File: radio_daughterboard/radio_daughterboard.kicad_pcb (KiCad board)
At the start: 4 copper layers, 120 x 40.5 mm, 126 parts, among them J1 DF40C 60-pin radio daughterbo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, J240 2m/VHF internal/PCB antenna f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, J241 2m/VHF rear external SMA/u.FL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, J250 70cm/UHF internal/PCB antenna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, J251 70cm/UHF rear external SMA/u.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, J42 GNSS passive antenna U.FL, J70 DRA818V 2m FM module, J71 DRA818U 70cm FM module, Q330 2N7002KT1G VHF PTT/suspend fa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, Q331 2N7002KT1G UHF PTT/suspend fa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, Q332 BSS84LT1G codec-loss force-mu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, U1 AP2112K-3.3 600mA daughterboa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, U240 PE42820B-X 2m/VHF 43dBm-CW RF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, U241 SN74LVC1G373DCKR VHF transmit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, U242 SN74LVC3G34DCUR VHF fail-safe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, U243 SN74LVC1T45 VHF TXD 4V-to-3V3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, U250 PE42820B-X 70cm/UHF 43dBm-CW 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, U251 SN74LVC1G373DCKR UHF transmit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, U252 SN74LVC3G34DCUR UHF fail-safe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, U253 SN74LVC1T45 UHF TXD 4V-to-3V3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, U260 SN74LVC2G04DCKR PTT request i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, U261 SN74LVC2G32DCUR dual-radio PT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, U330 PCM2902CDBR USB audio codec, U40 MAX-M10S GNSS, U41 SN74LVC3G34 GNSS input isolat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, U70 TPS54302 RADIO_DB_5V -> RADIO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, Y330 ABM8G-106-12.000MHZ-T 12MHz 1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

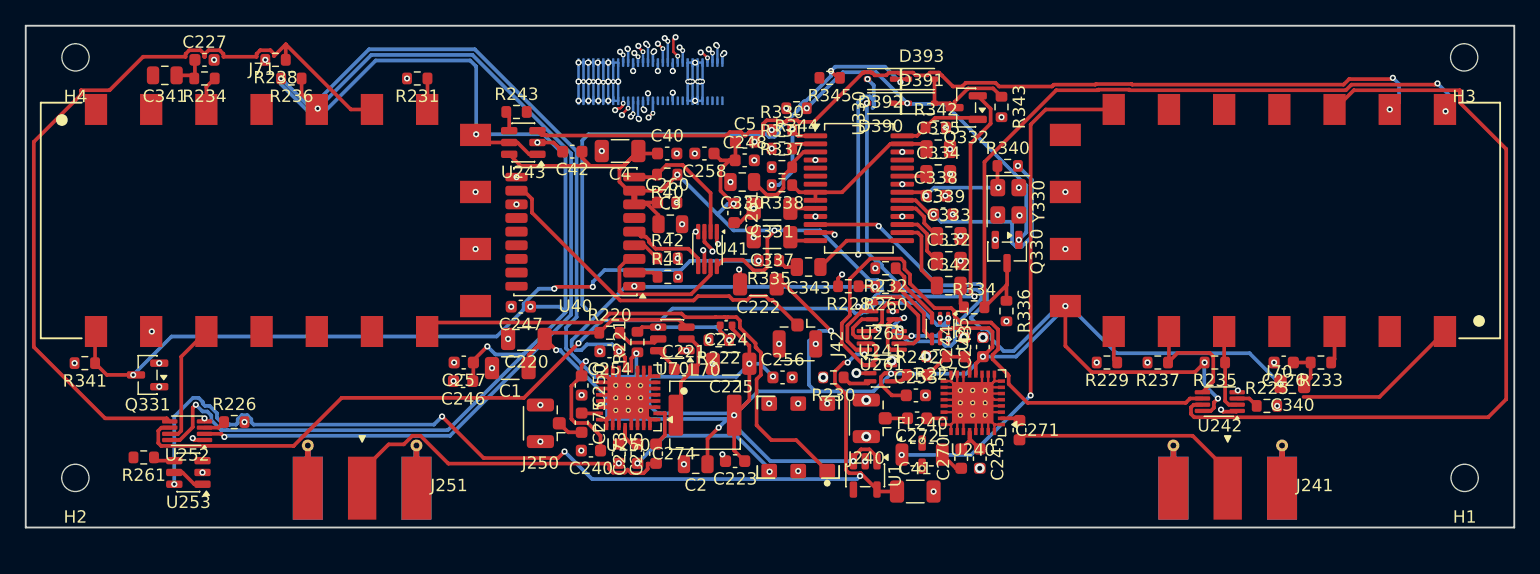
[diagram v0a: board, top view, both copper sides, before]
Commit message: Fix 3D model paths and update PCB format to KiCad 10.0
- Update 3D model paths in radio and keyboard daughterboards to use KIPRJMOD
- Replace Cherry MX ULP STEP model with corrected version
- Add Hirose DF40C and ublox MAX-7Q 3D STEP models
- Fix 3D model offset scripts for mezzanine connector stack
- Auto-format integer-to-float notation from KiCad 10.0 save
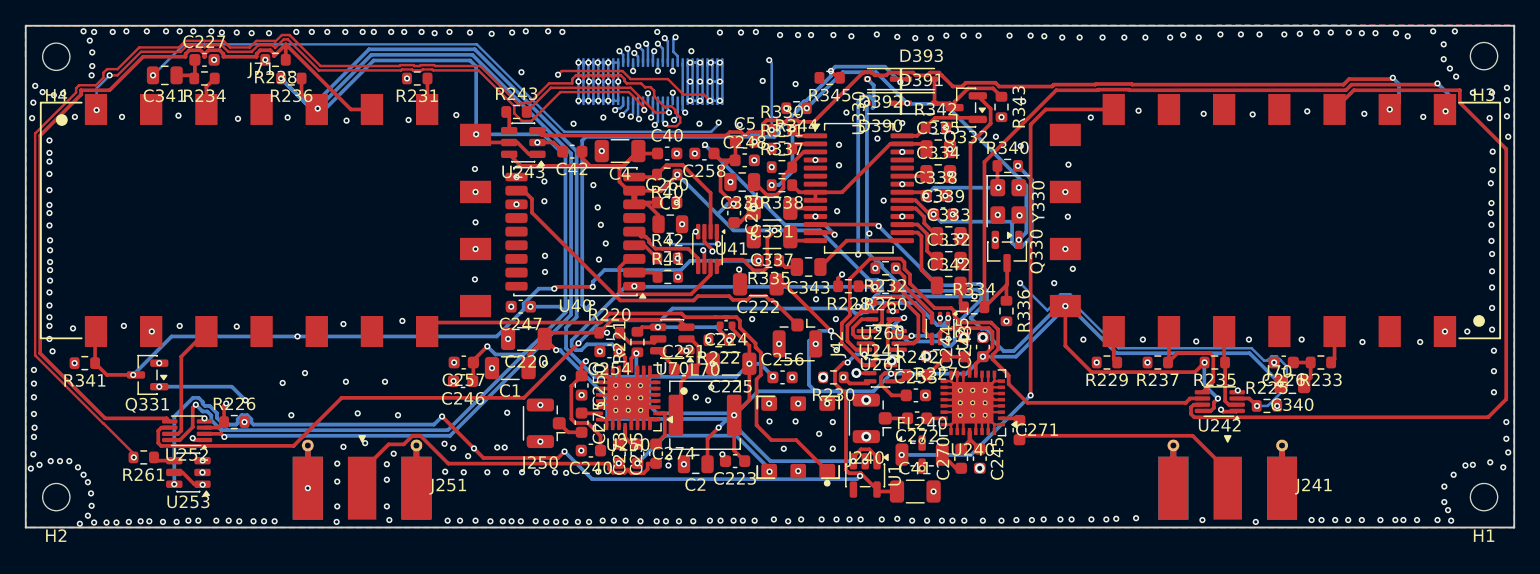
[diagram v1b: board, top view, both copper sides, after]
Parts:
- moved H1 2.20 mm to (207.7, 122.6)
- moved H2 2.18 mm to (92.6, 122.6)
- moved H3 1.60 mm to (207.7, 87.0)
- moved H4 1.55 mm to (92.6, 87.1)
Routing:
- net /RADIO_VHF_UART_TX: track 3.47 -> 102.2 mm
- net /RADIO_UHF_UART_RX: track 0.00 -> 95.8 mm, vias 0 -> 2
- net /RADIO_VHF_PD_N: track 3.32 -> 72.6 mm, vias 1 -> 3
- net /RADIO_VHF_SQL: track 15.1 -> 80.8 mm, vias 1 -> 2
- net /USB Radio Audio/CODEC_LINEIN_R: track 1.62 -> 67.3 mm, vias 1 -> 4
- net /RADIO_UHF_UART_TX: track 2.70 -> 65.4 mm
- net /RADIO_UHF_PD_N: track 3.34 -> 63.8 mm, vias 1 -> 2
- net /RADIO_VHF_RF_SEL_3V3: track 3.38 -> 61.6 mm, vias 1 -> 2
- net /RADIO_UHF_SQL: track 0.86 -> 53.9 mm, vias 1 -> 3
- net /RADIO_DB_5V: track 57.2 -> 105.0 mm, vias 7 -> 11
- net /USB Radio Audio/UHF_MUTE_GATE: track 45.5 -> 84.7 mm, vias 3 -> 5
- net /RADIO_UHF_RF_SEL_3V3: track 6.78 -> 35.2 mm, vias 1 -> 2
- net /GNSS_UART_TX: track 2.18 -> 29.7 mm, vias 2 -> 3
- net /RADIO_VHF_PTT_N: track 39.1 -> 66.4 mm, vias 2 -> 4
- net /GNSS_PPS: track 0.97 -> 24.6 mm
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- added copper zone on B.Cu, net GND
- added copper zone on F.Cu, net GND
- added copper zone on In2.Cu, net GND

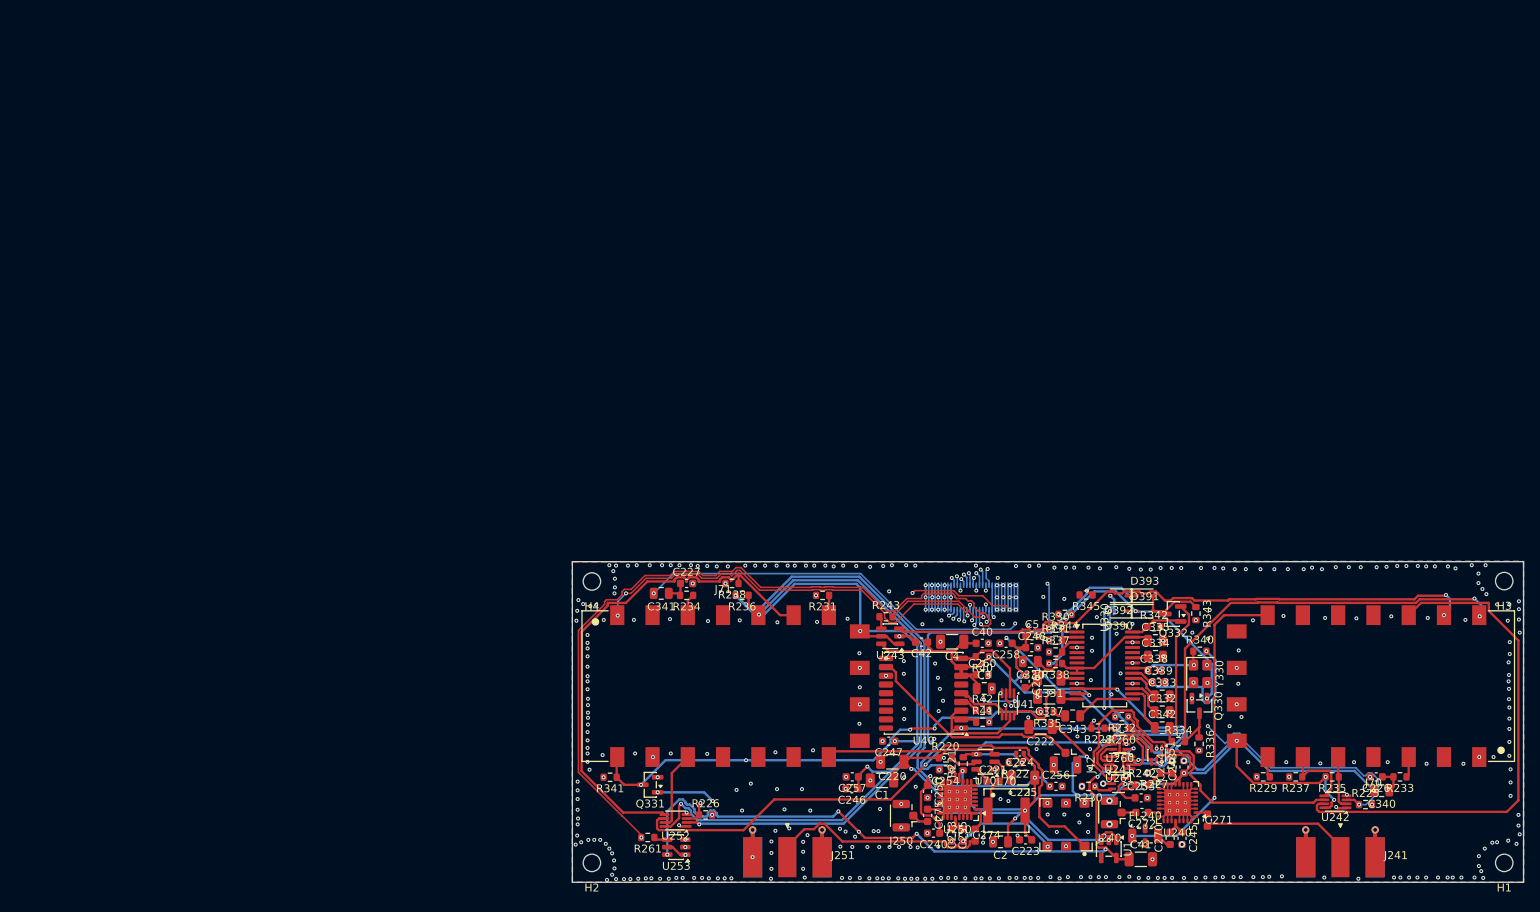
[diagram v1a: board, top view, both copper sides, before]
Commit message: Complete EC DFU port (J73) + DB power rework; verify schematic and board
- Add rear USB-C EC firmware programming port J73 (UFP/DFU) on Internal
  Services sheet: USBLC6-2P6 ESD (U63), 5.1k CC Rd resistors (R205/R211),
  22R series on D+/D- (R203/R204), mux-select hookup so BOOT0 high forces
  the USB mux to the DFU port
- Rename port ref J70->J73 after ham-radio collision; sync all net names
  (J73_CC1/J73_CC2)
- DB power rework: S5 gating + 3V3_STBY split, dual DCDC paths, GND
  returns on the standby rails; regenerate all sheets and re-verify
- sync_main_pcb_from_netlist: anchor placement for the 9 new footprints,
  scoped ECO support
- Board: rebuild main PCB with J73 footprint block (lib-sourced, net
  injection from netlist name attribute), sync pad nets for the 5 stale
  refs, remove duplicate R205/R211 copies
- Verified: check_schematic self-check OK (0 errors), radio DB contracts
  OK, ERC 0 errors, board DRC 0 electrical violations, board-vs-schematic
  net parity 0 conflicts, no duplicate refs
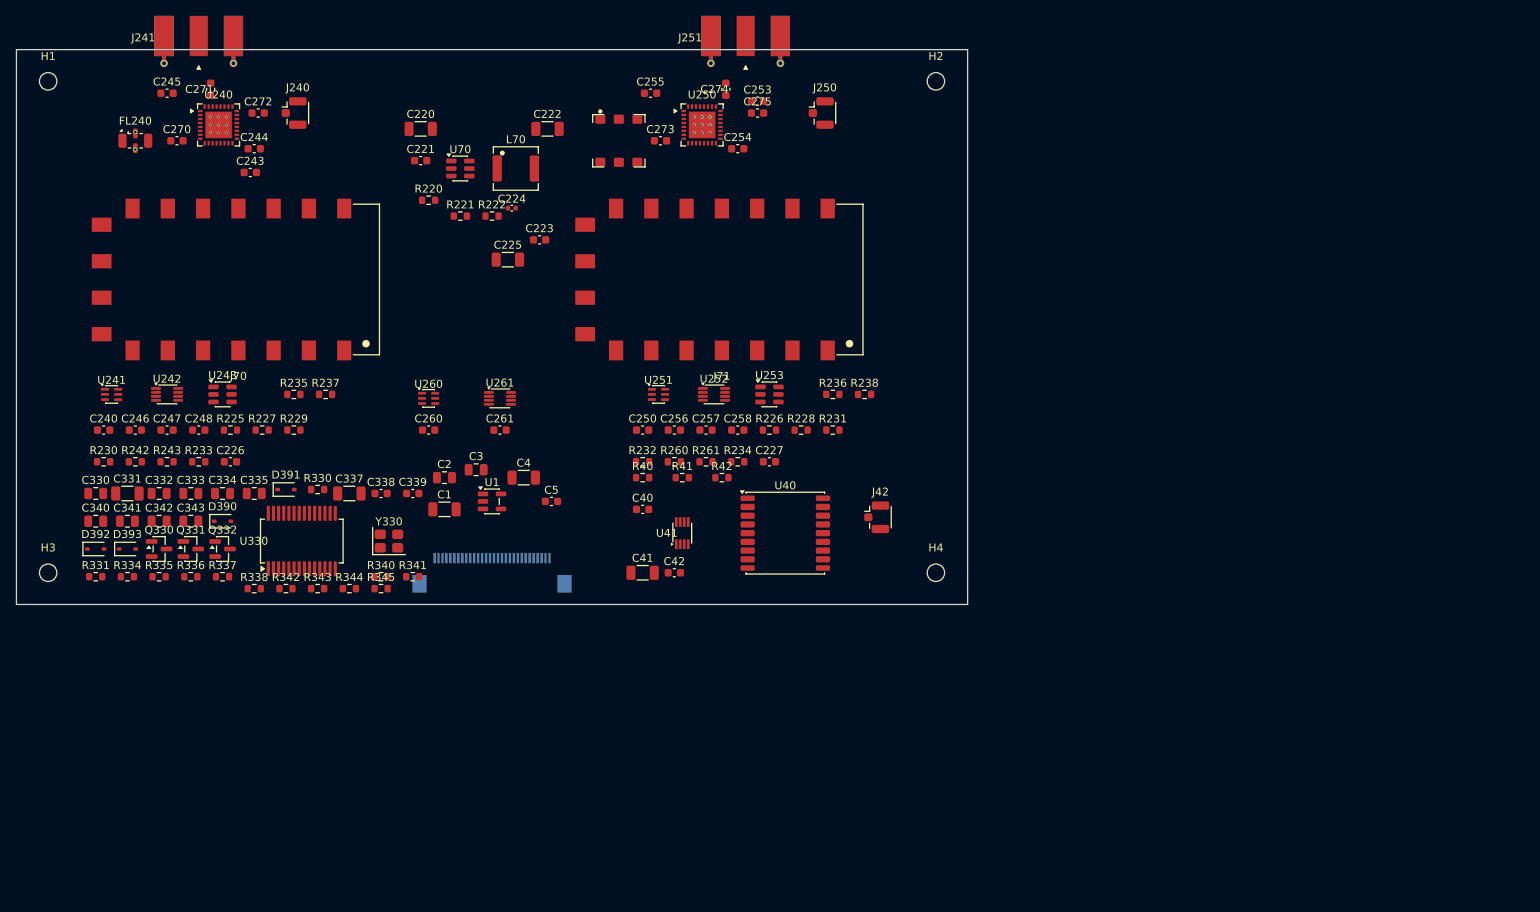
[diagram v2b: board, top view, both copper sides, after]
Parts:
- J1: value DF40C 60-pin radio daughterboard receptacle -> FH12-30S 30-pin radio daughterboard FFC; footprint Connector_Hirose_DF40:Hirose_DF40C(2.0)-60DS-0.4V_2x30_P0.4mm -> Connector_FFC-FPC:Hirose_FH12-30S-0.5SH_1x30-1MP_P0.50mm_Horizontal
- moved H1 208.5 mm to (24.0, 24.0), turned to 0 degrees
- moved H3 183.7 mm to (24.0, 86.0), turned to 0 degrees
- moved J241 175.4 mm to (43.0, 20.0), turned to -90 degrees
- moved C340 165.8 mm to (30.0, 79.5), turned to 0 degrees
- moved C245 158.8 mm to (39.0, 25.5), turned to 0 degrees
- moved R233 156.7 mm to (43.0, 72.0), turned to 0 degrees
- moved U242 156.1 mm to (39.0, 63.5), turned to 0 degrees
- moved C271 155.9 mm to (44.5, 25.0), turned to 90 degrees
- moved FL240 154.7 mm to (35.0, 31.5)
- moved C270 153.1 mm to (40.2, 31.5), turned to 0 degrees
- moved J70 152.1 mm to (48.0, 49.0)
- moved R225 150.8 mm to (47.0, 68.0)
- moved C226 149.9 mm to (47.0, 72.0), turned to 0 degrees
- moved U240 148.1 mm to (45.5, 29.5), turned to 0 degrees
- moved C272 142.2 mm to (50.5, 28.0), turned to 0 degrees
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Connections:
- J1 pad 1: /RADIO_DB_5V -> GND
- J1 pad 11: GND -> /RADIO_VHF_UART_TX
- J1 pad 12: GND -> /RADIO_VHF_UART_RX
- J1 pad 13: GND -> /RADIO_UHF_UART_TX
- J1 pad 14: GND -> /RADIO_UHF_UART_RX
- J1 pad 15: GND -> /RADIO_VHF_PTT_N
- J1 pad 16: GND -> /RADIO_UHF_PTT_N
- J1 pad 17: /RADIO_CODEC_USB_VBUS -> /RADIO_VHF_PD_N
- J1 pad 18: /RADIO_CODEC_USB_VBUS -> /RADIO_UHF_PD_N
- J1 pad 19: /RADIO_CODEC_USB_DP -> GND
- J1 pad 20: /RADIO_CODEC_USB_DM -> /RADIO_VHF_SQL
- J1 pad 21: GND -> /RADIO_UHF_SQL
- J1 pad 22: GND -> /RADIO_VHF_RF_SEL_3V3
- J1 pad 23: /RADIO_VHF_UART_TX -> /RADIO_UHF_RF_SEL_3V3
- J1 pad 24: /RADIO_VHF_UART_RX -> /GNSS_UART_RX
- J1 pad 25: /RADIO_UHF_UART_TX -> /GNSS_UART_TX
- J1 pad 26: /RADIO_UHF_UART_RX -> GND
- J1 pad 27: GND -> /GNSS_RESET_N
- J1 pad 28: /RADIO_VHF_PTT_N -> /GNSS_PPS
- J1 pad 29: /RADIO_UHF_PTT_N -> /GNSS_EXTINT
- J1 pad 30: /RADIO_VHF_PD_N -> GND
- J1 pad 4: /RADIO_DB_5V -> GND
- J1 pad 5: /RADIO_DB_5V -> /RADIO_CODEC_USB_VBUS
- J1 pad 7: /RADIO_DB_5V -> GND
- J1 pad 8: /RADIO_DB_5V -> /RADIO_CODEC_USB_DP
- J1 pad 9: GND -> /RADIO_CODEC_USB_DM
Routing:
- net /VHF & UHF Radios/RADIO_4V0: track 303.7 -> 0.00 mm, vias 17 -> 0
- net /RADIO_DB_3V3: track 184.9 -> 0.00 mm, vias 12 -> 0
- net GND: track 170.3 -> 0.00 mm, vias 465 -> 0
- net /RADIO_DB_5V: track 105.0 -> 0.00 mm, vias 11 -> 0
- net /RADIO_VHF_UART_TX: track 102.2 -> 0.00 mm, vias 2 -> 0
- net /RADIO_UHF_UART_RX: track 95.8 -> 0.00 mm, vias 2 -> 0
- net /USB Radio Audio/UHF_MUTE_GATE: track 84.7 -> 0.00 mm, vias 5 -> 0
- net /RADIO_VHF_SQL: track 80.8 -> 0.00 mm, vias 2 -> 0
- net /VHF & UHF Radios/RADIO_VHF_UART_TXD: track 76.9 -> 0.00 mm, vias 2 -> 0
- net /VHF & UHF Radios/RADIO_UHF_PTT_SAFE_N: track 76.8 -> 0.00 mm, vias 3 -> 0
- net /VHF & UHF Radios/RADIO_UHF_PTT_LOCAL_N: track 75.4 -> 0.00 mm, vias 2 -> 0
- net /RADIO_VHF_PD_N: track 72.6 -> 0.00 mm, vias 3 -> 0
- net /USB Radio Audio/CODEC_LINEIN_R: track 67.3 -> 0.00 mm, vias 4 -> 0
- net /RADIO_VHF_PTT_N: track 66.4 -> 0.00 mm, vias 4 -> 0
- net /VHF & UHF Radios/RADIO_UHF_PD_LOCAL_N: track 65.7 -> 0.00 mm
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- removed copper zone on B.Cu, net GND
- removed copper zone on F.Cu, net GND
- removed copper zone on In1.Cu, net GND
- removed copper zone on In2.Cu, net GND
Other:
- board size 120 x 40.5 mm -> 120 x 70 mm
- board text added: "DUCKTOP2 RADIO / GNSS DAUGHTERBOARD"
- board text added: "REAR / ANTENNA EDGE"

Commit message: get the main boards ready for routing
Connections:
- net /RADIO_CODEC_USB_DM renamed /RADIO_CODEC_USB_DN
- net /USB Radio Audio/CODEC_USB_DM renamed /USB Radio Audio/CODEC_USB_DN
- J70 pad 11: (no net) -> unconnected-(J70-NC-Pad11)
- J70 pad 13: (no net) -> unconnected-(J70-NC-Pad13)
- J70 pad 14: (no net) -> unconnected-(J70-NC-Pad14)
- J70 pad 15: (no net) -> unconnected-(J70-NC-Pad15)
- J70 pad 2: (no net) -> unconnected-(J70-NC-Pad2)
- J70 pad 4: (no net) -> unconnected-(J70-NC-Pad4)
- J71 pad 11: (no net) -> unconnected-(J71-NC-Pad11)
- J71 pad 13: (no net) -> unconnected-(J71-NC-Pad13)
- J71 pad 14: (no net) -> unconnected-(J71-NC-Pad14)
- J71 pad 15: (no net) -> unconnected-(J71-NC-Pad15)
- J71 pad 2: (no net) -> unconnected-(J71-NC-Pad2)
- J71 pad 4: (no net) -> unconnected-(J71-NC-Pad4)
- U1 pad 4: (no net) -> unconnected-(U1-NC-Pad4)
- U330 pad 24: (no net) -> unconnected-(U330-DIN-Pad24)
- U330 pad 25: (no net) -> unconnected-(U330-DOUT-Pad25)
- U330 pad 5: (no net) -> unconnected-(U330-HID0-Pad5)
- U330 pad 6: (no net) -> unconnected-(U330-HID1-Pad6)
- U330 pad 7: (no net) -> unconnected-(U330-HID2-Pad7)
- U40 pad 13: (no net) -> unconnected-(U40-LNA_EN-Pad13)
- U40 pad 14: (no net) -> unconnected-(U40-VCC_RF-Pad14)
- U40 pad 15: (no net) -> unconnected-(U40-VIO_SEL-Pad15)
- U40 pad 16: (no net) -> unconnected-(U40-SDA-Pad16)
- U40 pad 17: (no net) -> unconnected-(U40-SCL-Pad17)
- U40 pad 18: (no net) -> unconnected-(U40-~{SAFEBOOT}-Pad18)
- U40 pad 6: (no net) -> unconnected-(U40-V_BCKP-Pad6)

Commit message: fix audit issues and move some connectors
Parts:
- moved C253 10.1 mm to (107.0, 34.2)
- moved C274 7.99 mm to (102.4, 28.6)
- moved J251 5.84 mm to (108.0, 24.3)
- moved C271 4.63 mm to (41.6, 28.6)
- moved J241 4.26 mm to (43.0, 24.3)
- moved C245 3.09 mm to (39.8, 28.5), turned to 90 degrees
- moved U240 0.70 mm to (45.5, 30.2)
- moved U250 0.70 mm to (106.5, 30.2)
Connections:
- J70 pad 11: unconnected-(J70-NC-Pad11) -> (no net)
- J70 pad 13: unconnected-(J70-NC-Pad13) -> (no net)
- J70 pad 14: unconnected-(J70-NC-Pad14) -> (no net)
- J70 pad 15: unconnected-(J70-NC-Pad15) -> (no net)
- J70 pad 2: unconnected-(J70-NC-Pad2) -> (no net)
- J70 pad 4: unconnected-(J70-NC-Pad4) -> (no net)
- J71 pad 11: unconnected-(J71-NC-Pad11) -> (no net)
- J71 pad 13: unconnected-(J71-NC-Pad13) -> (no net)
- J71 pad 14: unconnected-(J71-NC-Pad14) -> (no net)
- J71 pad 15: unconnected-(J71-NC-Pad15) -> (no net)
- J71 pad 2: unconnected-(J71-NC-Pad2) -> (no net)
- J71 pad 4: unconnected-(J71-NC-Pad4) -> (no net)
- U1 pad 4: unconnected-(U1-NC-Pad4) -> (no net)
- U330 pad 24: unconnected-(U330-DIN-Pad24) -> (no net)
- U330 pad 25: unconnected-(U330-DOUT-Pad25) -> (no net)
- U330 pad 5: unconnected-(U330-HID0-Pad5) -> (no net)
- U330 pad 6: unconnected-(U330-HID1-Pad6) -> (no net)
- U330 pad 7: unconnected-(U330-HID2-Pad7) -> (no net)
- U40 pad 13: unconnected-(U40-LNA_EN-Pad13) -> (no net)
- U40 pad 14: unconnected-(U40-VCC_RF-Pad14) -> (no net)
- U40 pad 15: unconnected-(U40-VIO_SEL-Pad15) -> (no net)
- U40 pad 16: unconnected-(U40-SDA-Pad16) -> (no net)
- U40 pad 17: unconnected-(U40-SCL-Pad17) -> (no net)
- U40 pad 18: unconnected-(U40-~{SAFEBOOT}-Pad18) -> (no net)
- U40 pad 6: unconnected-(U40-V_BCKP-Pad6) -> (no net)
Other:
- board text added: "ducktop2 radio / gnss"
- board text removed: "DUCKTOP2 RADIO / GNSS DAUGHTERBOARD"
